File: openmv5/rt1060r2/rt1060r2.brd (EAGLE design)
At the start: 35.6 x 44.5 mm, 258 parts, among them CN1 S2B-PH-K-S(LF)(SN), IC1 LM66200DRLR, IC2 TCR2LF33,LM_CT, IC3 AP61300Z6-7, IC4 IS42S16160G-6BL, IC5 IS25LP128F-JKLE-TR, IC6 SE050C1HQ1_Z01SCZ, IC7 MXC4005XC, IC8 KSZ8081RNDCA-TR, IC9 MIMXRT106FCVL5B, J1 USB4105-GF-A, J2 USD-1040310811, J3 DF12-36-DS, J4 DNP, J5 DNP, J6 DNP, J7 DNP, J8 3221-10-0300-00, J9 DNP, M1 9774030151R, M2 9774030151R, Q1 DMG2301L-7, Q2 2N7002KW_R1_00001, Q3 2N7002KW_R1_00001, Q4 2N7002KW_R1_00001, U1 BQ24075RGTR, U2 LBEE5KL1DX-883, Y1 ECS-327MVATX-3-CN-TR3, Y2 XRCGB24M000F3M00R0, Y3 SC32S-7PF20PPM

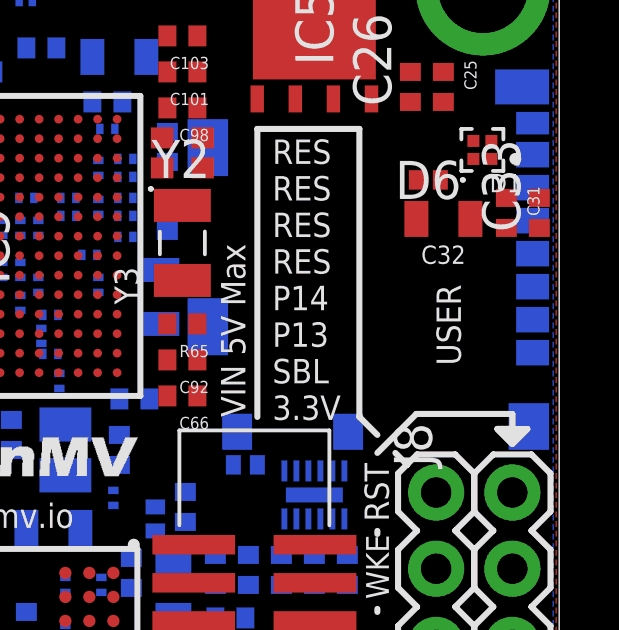
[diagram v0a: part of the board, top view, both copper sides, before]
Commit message: Fix some issues with MPN and extra lablels
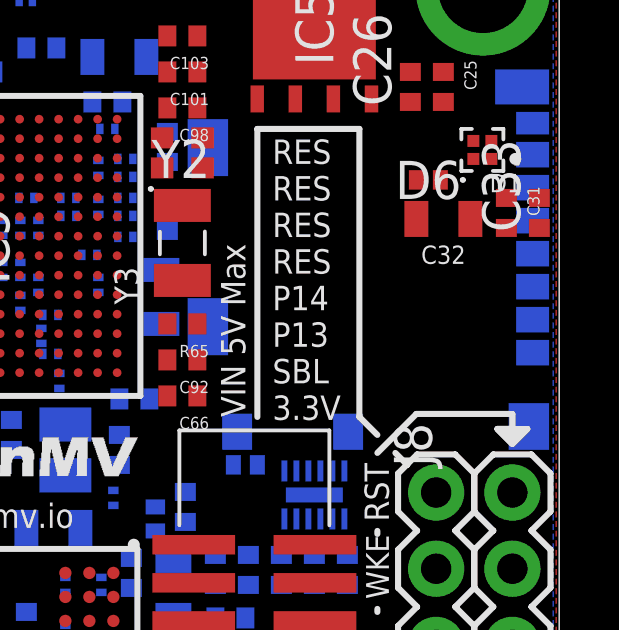
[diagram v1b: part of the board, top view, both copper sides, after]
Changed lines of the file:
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@@
 <wire x1="29.5" y1="15.4" x2="29.5" y2="15.5" width="0.2032" layer="21"/>
 <wire x1="29.5" y1="18" x2="29.5" y2="18.1" width="0.2032" layer="21"/>
-<text x="32.285" y="23.615" size="0.8128" layer="21" font="vector" ratio="20" rot="R90">USER</text>
 <wire x1="18.2" y1="4.4" x2="18.2" y2="3.6" width="0.2032" layer="22"/>
 <wire x1="17.8" y1="4" x2="18.6" y2="4" width="0.2032" layer="22"/>
@@
 </element>
 <element name="R42" library="0402" package="0402" value="1K" x="16.4" y="39.9" smashed="yes" rot="MR270">
-<attribute name="MPN" value="AC0402FR-1310KL" x="16.4" y="39.9" size="1.778" layer="28" rot="MR270" display="off"/>
+<attribute name="MPN" value="CRCW04021K00FKEDC" x="16.4" y="39.9" size="1.778" layer="28" rot="MR270" display="off"/>
 <attribute name="NAME" x="15.865" y="40.535" size="0.8128" layer="26" ratio="10" rot="MR270"/>
 <attribute name="VALUE" x="17.805" y="40.535" size="0.8128" layer="28" ratio="10" rot="MR270"/>
 </element>
 <element name="R43" library="0402" package="0402" value="1K" x="17.5" y="39.9" smashed="yes" rot="MR270">
-<attribute name="MPN" value="AC0402FR-1310KL" x="17.5" y="39.9" size="1.778" layer="28" rot="MR270" display="off"/>
+<attribute name="MPN" value="CRCW04021K00FKEDC" x="17.5" y="39.9" size="1.778" layer="28" rot="MR270" display="off"/>
 <attribute name="NAME" x="16.965" y="40.535" size="0.8128" layer="26" ratio="10" rot="MR270"/>
 <attribute name="VALUE" x="18.905" y="40.535" size="0.8128" layer="28" ratio="10" rot="MR270"/>
@@
 <attribute name="MOUSER_PART_NUMBER" value="771-SE050C1HQ1Z01SCZ" x="11.6" y="35.5" size="1.778" layer="28" rot="MR0" display="off"/>
 <attribute name="MOUSER_PRICE-STOCK" value="https://www.mouser.co.uk/ProductDetail/NXP-Semiconductors/SE050C1HQ1-Z01SCZ?qs=uwxL4vQweFPAe9Cpm7Fm%252BQ%3D%3D" x="11.6" y="35.5" size="1.778" layer="28" rot="MR0" display="off"/>
+<attribute name="MPN" value="SE050C1HQ1/Z01SCZ" x="11.6" y="35.5" size="1.778" layer="28" rot="MR0" display="off"/>
 <attribute name="NAME" x="11.6" y="35.5" size="1.27" layer="26" rot="MR0" align="center"/>
 <attribute name="VALUE" x="11.6" y="35.5" size="1.27" layer="28" rot="MR0" align="center"/>

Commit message: Update diodes
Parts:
- removed D3, D4: RB521S30T5G, RB521S30T5G:SODFL1608X70N
- added C113: 4.7uF, 0402:0402
- added D15: BAT54CLT3G, BAT54CLT3G:SOT96P237X111-3N
- moved TP1 23.1 mm to (33.0, 22.8), flipped to the top
- moved TP2 21.0 mm to (31.0, 22.8), flipped to the top
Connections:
- net GND: now also C113.1
- net SNVS_BAT: now also D15.2; no longer D4.2
- net VCC: now also C113.2
- net VDD_SNVS: now also D15.1; no longer D3.2
- net VDD_SNVS_CPU: now also D15.3; no longer D3.1, D4.1

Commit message: Fix possible low power mode leakage
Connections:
- net VDD_SNVS: no longer Q2.1, Q3.1, Q4.1
- net VDD_SNVS_CPU: now also Q2.1, Q3.1, Q4.1
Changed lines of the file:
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@@
 </signal>
 <signal name="VDD_SNVS">
-<contactref element="Q2" pad="1"/>
-<contactref element="Q3" pad="1"/>
-<contactref element="Q4" pad="1"/>
 <contactref element="C9" pad="2"/>
 <contactref element="IC2" pad="5"/>
 <contactref element="D15" pad="1"/>
-<wire x1="15.7" y1="5.25" x2="24.65" y2="11.8" width="0" layer="19" extent="16-16"/>
+<wire x1="15.7" y1="5.25" x2="31.045" y2="24.4" width="0" layer="19" extent="1-16"/>
 <wire x1="16.4" y1="4.1" x2="15.7" y2="5.25" width="0" layer="19" extent="16-16"/>
-<wire x1="10.9" y1="7.65" x2="15.7" y2="5.25" width="0" layer="19" extent="16-16"/>
-<wire x1="9.5" y1="8.95" x2="10.9" y2="7.65" width="0" layer="19" extent="16-16"/>
-<wire x1="31.045" y1="24.4" x2="9.5" y2="8.95" width="0" layer="19" extent="1-16"/>
 </signal>
 <signal name="VDD_HIGH_CAP">
@@
 <contactref element="C86" pad="1"/>
 <contactref element="D15" pad="3"/>
+<contactref element="Q2" pad="1"/>
+<contactref element="Q3" pad="1"/>
+<contactref element="Q4" pad="1"/>
+<wire x1="19.525" y1="28.575" x2="32" y2="26.8" width="0" layer="19" extent="1-1"/>
 <wire x1="19.45" y1="28.6" x2="19.525" y2="28.575" width="0" layer="19" extent="1-16"/>
-<wire x1="32" y1="26.8" x2="19.45" y2="28.6" width="0" layer="19" extent="1-16"/>
+<wire x1="24.65" y1="11.8" x2="32" y2="26.8" width="0" layer="19" extent="1-16"/>
+<wire x1="10.9" y1="7.65" x2="24.65" y2="11.8" width="0" layer="19" extent="16-16"/>
+<wire x1="9.5" y1="8.95" x2="10.9" y2="7.65" width="0" layer="19" extent="16-16"/>
 </signal>
 <signal name="JTAG_TRSTB_INT_UNUSED">

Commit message: Update processor
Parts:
- IC9: value MIMXRT106FCVL5B -> MIMXRT106FDVL6B
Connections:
- net RST_BUTTON renamed ONOFF_BUTTON
- net ONOFF: now also R70.1
- net P12_RST_N: no longer R70.1
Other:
- board text added: "ON/OFF"
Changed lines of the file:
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@@
 <wire x1="29.4" y1="22.8" x2="30.2" y2="22.8" width="0.2032" layer="22"/>
 <text x="9.4" y="44.3" size="0.8128" layer="22" font="vector" ratio="20" rot="MR270">USER</text>
-<text x="27" y="44.3" size="0.8128" layer="22" font="vector" ratio="20" rot="MR270">RST</text>
+<text x="27" y="44.3" size="0.8128" layer="22" font="vector" ratio="20" rot="MR270">ON/OFF</text>
 </plain>
 <attributes>
@@
 <attribute name="VALUE" x="2.843" y="27.8205" size="0.4064" layer="27" rot="R90"/>
 </element>
-<element name="IC9" library="MIMXRT1052DVL6B" package="BGA196C65P14X14_1000X1000X143" value="MIMXRT106FCVL5B" x="16.6" y="27.6" smashed="yes" rot="R90">
-<attribute name="DESCRIPTION" value="Processors - Application Specialized MIMXRT1062DVL6B/LFBGA196///STANDARD MARKING * TRAY" x="16.6" y="27.6" size="1.778" layer="27" rot="R90" display="off"/>
+<element name="IC9" library="MIMXRT1052DVL6B" package="BGA196C65P14X14_1000X1000X143" value="MIMXRT106FDVL6B" x="16.6" y="27.6" smashed="yes" rot="R90">
+<attribute name="DESCRIPTION" value="Processors - Application Specialized MIMXRT106FDVL6B/LFBGA196///STANDARD MARKING * TRAY" x="16.6" y="27.6" size="1.778" layer="27" rot="R90" display="off"/>
 <attribute name="HEIGHT" value="1.43mm" x="16.6" y="27.6" size="1.778" layer="27" rot="R90" display="off"/>
 <attribute name="MANUFACTURER_NAME" value="NXP" x="16.6" y="27.6" size="1.778" layer="27" rot="R90" display="off"/>
-<attribute name="MANUFACTURER_PART_NUMBER" value="MIMXRT1062DVL6B" x="16.6" y="27.6" size="1.778" layer="27" rot="R90" display="off"/>
-<attribute name="MOUSER_PART_NUMBER" value="771-MIMXRT1062DVL6B" x="16.6" y="27.6" size="1.778" layer="27" rot="R90" display="off"/>
-<attribute name="MOUSER_PRICE-STOCK" value="https://www.mouser.co.uk/ProductDetail/NXP-Semiconductors/MIMXRT1062DVL6B" x="16.6" y="27.6" size="1.778" layer="27" rot="R90" display="off"/>
-<attribute name="MPN" value="MIMXRT106FCVL5B" x="16.6" y="27.6" size="1.778" layer="27" rot="R90" display="off"/>
+<attribute name="MANUFACTURER_PART_NUMBER" value="MIMXRT106FDVL6B" x="16.6" y="27.6" size="1.778" layer="27" rot="R90" display="off"/>
+<attribute name="MOUSER_PART_NUMBER" value="771-MIMXRT106FDVL6B" x="16.6" y="27.6" size="1.778" layer="27" rot="R90" display="off"/>
+<attribute name="MOUSER_PRICE-STOCK" value="https://www.mouser.co.uk/ProductDetail/NXP-Semiconductors/MIMXRT106FDVL6B" x="16.6" y="27.6" size="1.778" layer="27" rot="R90" display="off"/>
+<attribute name="MPN" value="MIMXRT106FDVL6B" x="16.6" y="27.6" size="1.778" layer="27" rot="R90" display="off"/>
 <attribute name="NAME" x="16.6" y="27.6" size="1.27" layer="25" rot="R90" align="center"/>
 <attribute name="VALUE" x="16.6" y="27.6" size="1.27" layer="27" rot="R90" align="center"/>
@@
 <contactref element="R65" pad="2"/>
 <contactref element="FL5" pad="2"/>
-<contactref element="R70" pad="1"/>
 <wire x1="19.65" y1="27.3" x2="19.525" y2="27.275" width="0" layer="19" extent="1-16"/>
 <wire x1="22.5" y1="25" x2="19.65" y2="27.3" width="0" layer="19" extent="1-16"/>
 <wire x1="26.7" y1="10.5" x2="22.5" y2="25" width="0" layer="19" extent="1-16"/>
-<wire x1="26.4" y1="39.5" x2="26.7" y2="10.5" width="0" layer="19" extent="1-16"/>
 </signal>
 <signal name="JTAG_TRSTB_INT" class="4">
@@
 <contactref element="Q3" pad="2"/>
 <contactref element="IC9" pad="M6"/>
+<contactref element="R70" pad="1"/>
+<wire x1="19.525" y1="26.625" x2="26.4" y2="39.5" width="0" layer="19" extent="1-1"/>
 <wire x1="9.5" y1="7.65" x2="19.525" y2="26.625" width="0" layer="19" extent="1-16"/>
 </signal>
@@
 <wire x1="29.6" y1="9.3" x2="31.46" y2="9.22" width="0" layer="19" extent="16-16"/>
 </signal>
-<signal name="RST_BUTTON">
+<signal name="ONOFF_BUTTON">
 <contactref element="S2" pad="3"/>
 <contactref element="S2" pad="2"/>
 <contactref element="S2" pad="4"/>
 <contactref element="R70" pad="2"/>
-<wire x1="28.45" y1="42.2" x2="26.4" y2="40.5" width="0" layer="19" extent="1-1"/>
 <wire x1="26.4" y1="41.575" x2="28.45" y2="42.2" width="0" layer="19" extent="1-1"/>
+<wire x1="26.4" y1="40.5" x2="26.4" y2="41.575" width="0" layer="19" extent="1-1"/>
 <wire x1="24.35" y1="42.2" x2="26.4" y2="41.575" width="0" layer="19" extent="1-1"/>
 </signal>
